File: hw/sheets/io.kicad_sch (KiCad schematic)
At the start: 10 parts, among them J2 TYPE-C-31-M-12, J3 TE_292303-7, J4 Hirose_DM3D-SF, J5 Wuerth_694106301002, J6 AudioJack4_Ground, J7 SFW15R-2STE1LF, J8 SFW15R-2STE1LF

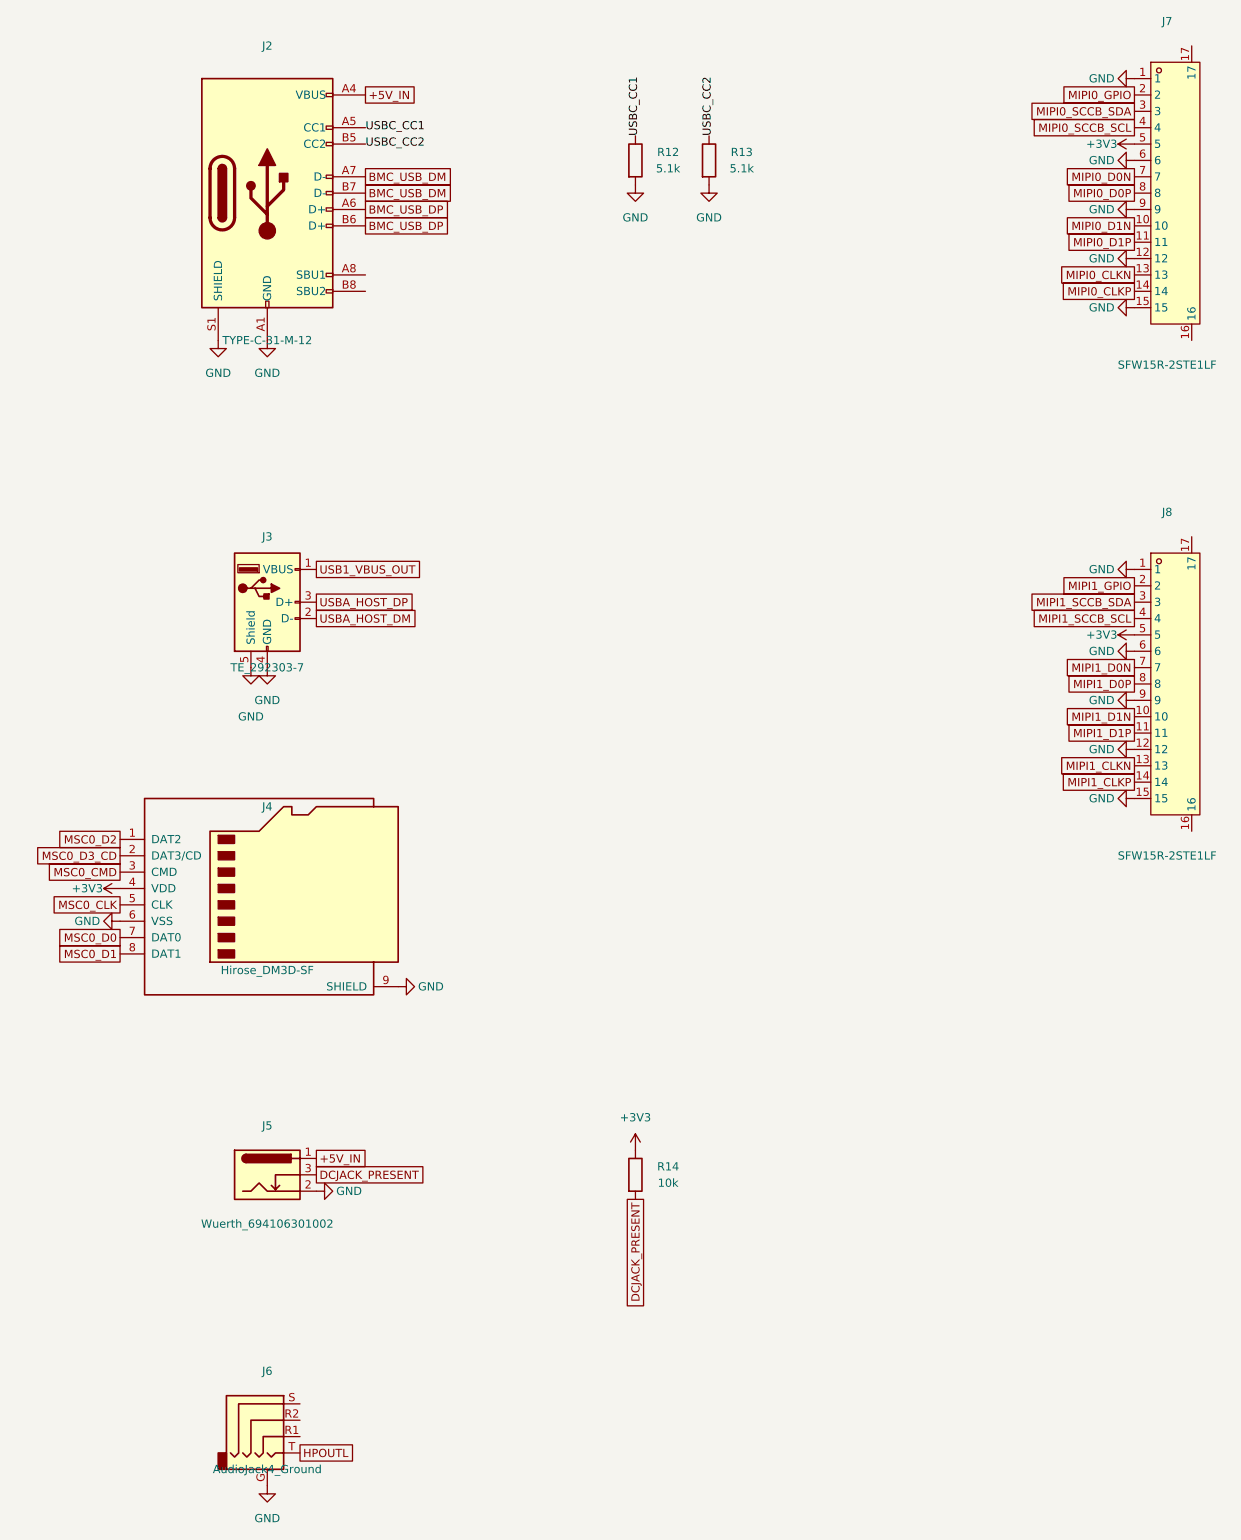
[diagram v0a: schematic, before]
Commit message: Carrier board: BMC power isolation, ESP-Hosted link, GPIO expander
Rebuilds the schematic to connectivity-by-label per BUILD.md (zero
wires/junctions) across all four sections, and adds the BMC power
architecture, connector crossings, and safety fixes worked out this
session:

- Dedicated BMC USB-C (J9), isolated 5V domains (+5V_BMC/+5V_ALT/+5V_SW),
  priority DC-jack-over-USB-C P-FET OR (Q1/Q2), 2:1 load-switch select
  (U4/U14) with a genuine ON-OFF-ON manual override (SW2)
- D1/D2 diode-OR so the BMC stays powered on ALT-only input without
  reopening the J9 backfeed path
- JP1 provisioning jumper + mandatory bring-up checklist: gates SW2 until
  the digipot's NV memory has been confirmed safe, closing the
  factory-mid-scale-default overvoltage gap on VCORE
- GPIO expander (U15, TCA9555PWR) frees 9 ESP32 GPIOs for a full-duplex
  SPI link to the interposer SoC (ESP-Hosted WiFi/BLE co-processor),
  while keeping flash chip-select and power-domain switching native for
  margin testing
- microSD, headphone jack, and both MIPI camera FFCs now cross the DDR4
  connector to the interposer, with GND isolation around each block
- J2/J3 share one USB host data pair to the interposer (peripheral use,
  independent of J2's power role)
- Added missing primary SOIC-8 NOR flash chip (W25Q32JVSS) to match the
  reference board's dual-NOR layout

docs/UNIVERSAL.md updated throughout to match; CONNECTIONS.txt and the
ESP32 pinout reference regenerated from the current netlist.
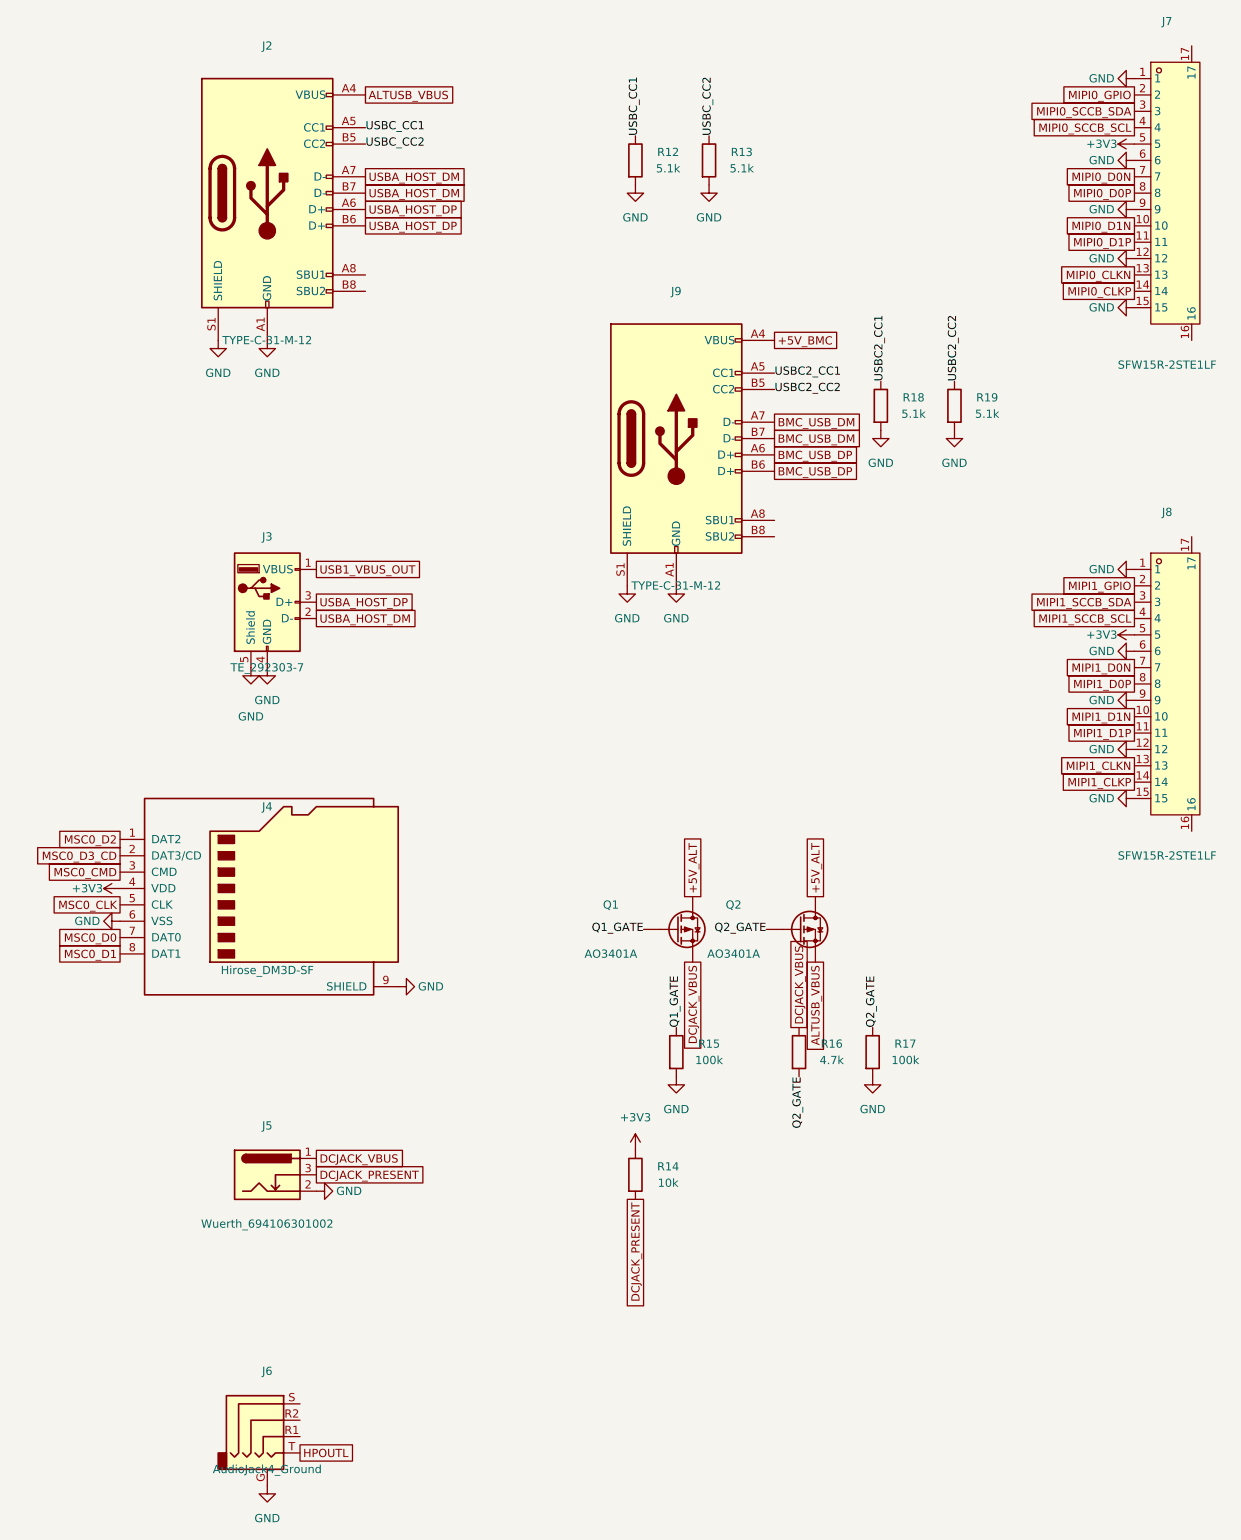
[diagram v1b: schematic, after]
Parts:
- added J9: TYPE-C-31-M-12, Connector_USB:USB_C_Receptacle_HRO_TYPE-C-31-M-12, symbol Connector:USB_C_Receptacle_USB2.0_16P
- added Q1, Q2: AO3401A, Package_TO_SOT_SMD:SOT-23, symbol Device:Q_PMOS
- added R15, R17: 100k, Resistor_SMD:R_0402_1005Metric, symbol Device:R
- added R16: 4.7k, Resistor_SMD:R_0402_1005Metric, symbol Device:R
- added R18, R19: 5.1k, Resistor_SMD:R_0402_1005Metric, symbol Device:R
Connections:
- net BMC_USB_DM: now also J9.A7 (D-), J9.B7 (D-); no longer J2.A7 (D-), J2.B7 (D-)
- net BMC_USB_DP: now also J9.A6 (D+), J9.B6 (D+); no longer J2.A6 (D+), J2.B6 (D+)
- net GND: now also J9.A1 (GND), J9.A12 (GND), J9.B1 (GND), J9.B12 (GND), J9.S1 (SHIELD), R15.2, R17.2, R18.2, R19.2
- net USBA_HOST_DM: now also J2.A7 (D-), J2.B7 (D-)
- net USBA_HOST_DP: now also J2.A6 (D+), J2.B6 (D+)
- net +5V_IN renamed ALTUSB_VBUS
- net ALTUSB_VBUS: now also Q2.S; no longer J5.1
- new net +5V_ALT: Q1.D, Q2.D
- new net +5V_BMC: J9.A4 (VBUS), J9.A9 (VBUS), J9.B4 (VBUS), J9.B9 (VBUS)
- new net DCJACK_VBUS: J5.1, Q1.S, R16.1
- new net Q1_GATE: Q1.G, R15.1
- new net Q2_GATE: Q2.G, R16.2, R17.1
- new net USBC2_CC1: J9.A5 (CC1), R18.1
- new net USBC2_CC2: J9.B5 (CC2), R19.1
